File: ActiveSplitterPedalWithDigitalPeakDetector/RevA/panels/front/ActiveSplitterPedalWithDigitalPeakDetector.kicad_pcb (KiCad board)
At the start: 2 copper layers, 112.5 x 86.4 mm, 5 parts

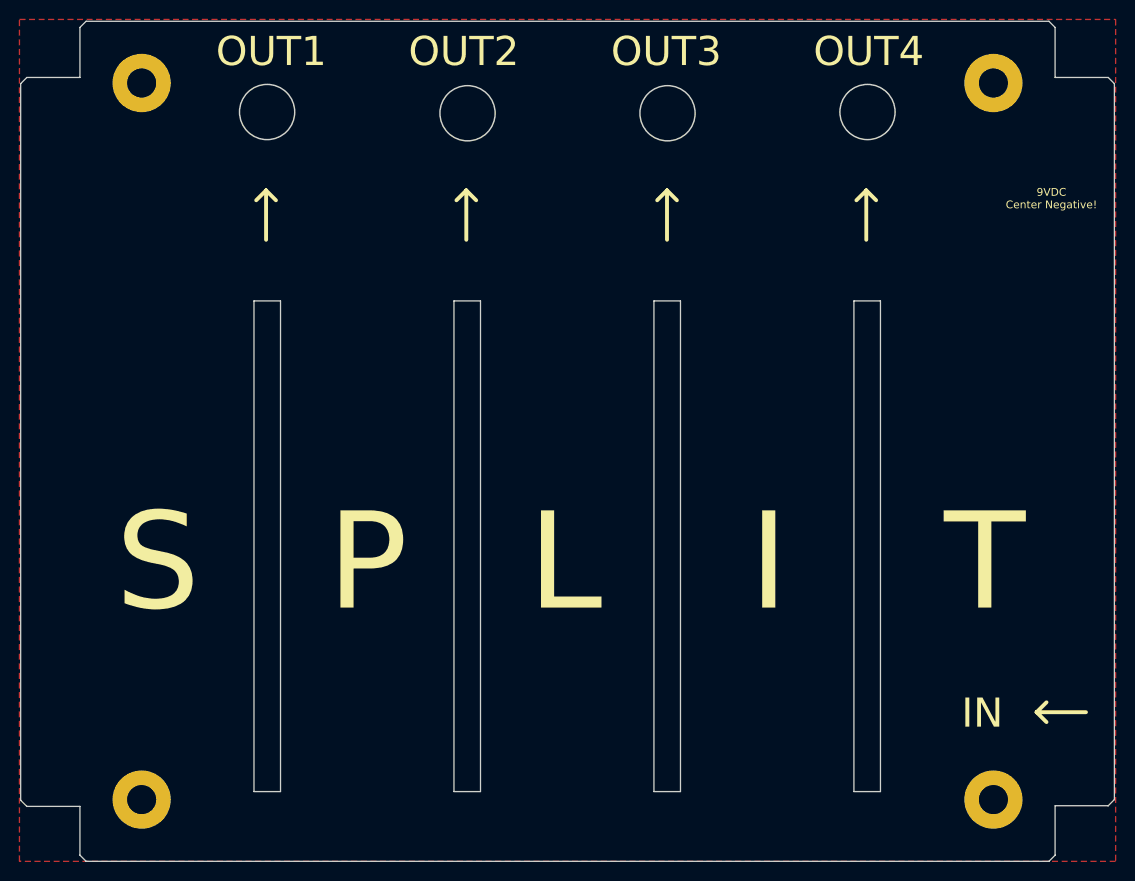
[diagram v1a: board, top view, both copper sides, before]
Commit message: updated front panel layout
moved silk screen
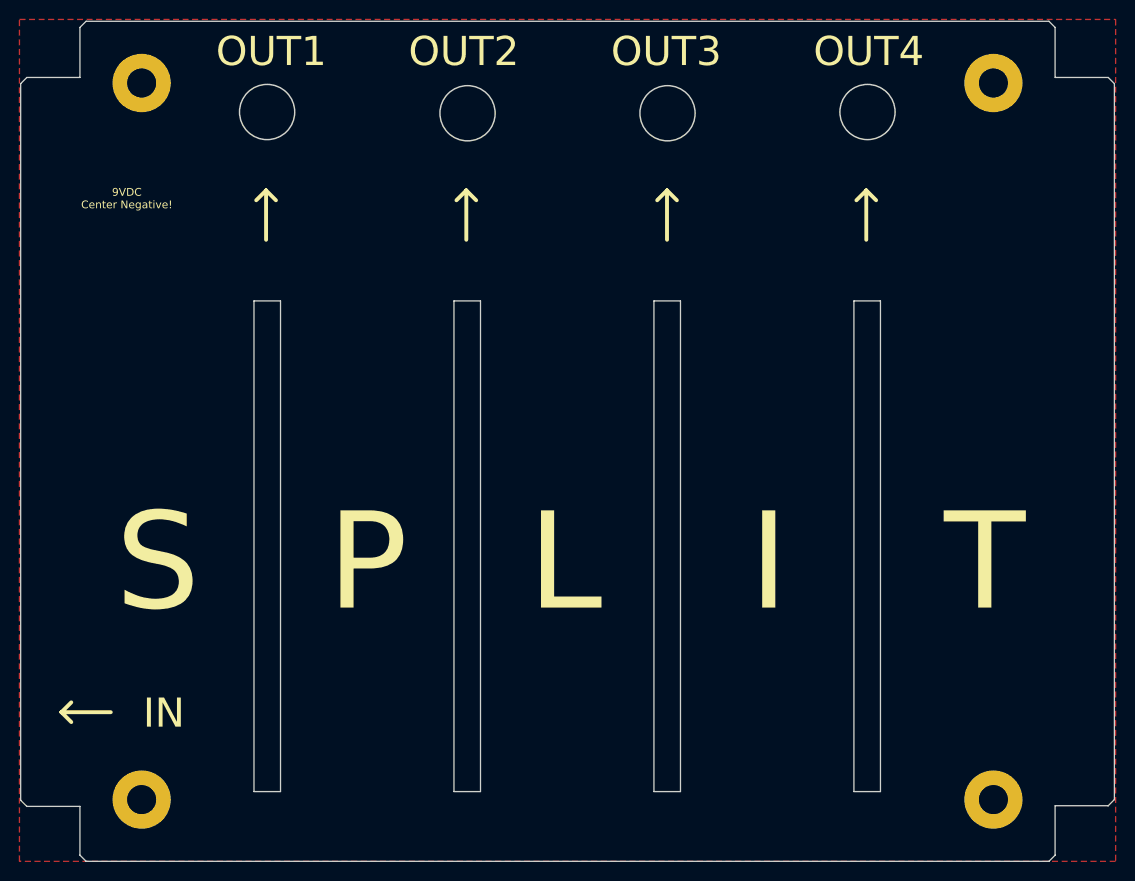
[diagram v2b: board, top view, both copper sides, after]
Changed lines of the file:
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@@
-(kicad_pcb (version 20171130) (host pcbnew "(5.1.6-0-10_14)")
+(kicad_pcb (version 20171130) (host pcbnew 5.1.6-c6e7f7d~87~ubuntu18.04.1)
   (general
     (thickness 1.6)
@@
       (effects (font (size 1 1) (thickness 0.15)))
     )
-    (fp_circle (center 0 0) (end 3.25 0) (layer F.CrtYd) (width 0.05))
-    (fp_circle (center 0 0) (end 3 0) (layer Cmts.User) (width 0.15))
+    (fp_circle (center 0 0) (end 3 0) (layer Cmts.User) (width 0.15))
+    (fp_circle (center 0 0) (end 3.25 0) (layer F.CrtYd) (width 0.05))
     (fp_text user %R (at 0.3 0) (layer F.Fab)
       (effects (font (size 1 1) (thickness 0.15)))
@@
       (effects (font (size 1 1) (thickness 0.15)))
     )
-    (fp_circle (center 0 0) (end 3.25 0) (layer F.CrtYd) (width 0.05))
-    (fp_circle (center 0 0) (end 3 0) (layer Cmts.User) (width 0.15))
+    (fp_circle (center 0 0) (end 3 0) (layer Cmts.User) (width 0.15))
+    (fp_circle (center 0 0) (end 3.25 0) (layer F.CrtYd) (width 0.05))
     (fp_text user %R (at 0.3 0) (layer F.Fab)
       (effects (font (size 1 1) (thickness 0.15)))
@@
       (effects (font (size 1 1) (thickness 0.15)))
     )
-    (fp_circle (center 0 0) (end 3.25 0) (layer F.CrtYd) (width 0.05))
-    (fp_circle (center 0 0) (end 3 0) (layer Cmts.User) (width 0.15))
+    (fp_circle (center 0 0) (end 3 0) (layer Cmts.User) (width 0.15))
+    (fp_circle (center 0 0) (end 3.25 0) (layer F.CrtYd) (width 0.05))
     (fp_text user %R (at 0.3 0) (layer F.Fab)
       (effects (font (size 1 1) (thickness 0.15)))
@@
       (effects (font (size 1 1) (thickness 0.15)))
     )
-    (fp_circle (center 0 0) (end 3.25 0) (layer F.CrtYd) (width 0.05))
-    (fp_circle (center 0 0) (end 3 0) (layer Cmts.User) (width 0.15))
+    (fp_circle (center 0 0) (end 3 0) (layer Cmts.User) (width 0.15))
+    (fp_circle (center 0 0) (end 3.25 0) (layer F.CrtYd) (width 0.05))
     (fp_text user %R (at 0.3 0) (layer F.Fab)
       (effects (font (size 1 1) (thickness 0.15)))
@@
       (effects (font (size 1 1) (thickness 0.15)))
     )
+    (fp_line (start 43.2435 -49.53) (end 42.6085 -50.165) (layer Dwgs.User) (width 0.12))
+    (fp_line (start 36.83 -56.261) (end 37.465 -55.626) (layer Dwgs.User) (width 0.12))
+    (fp_line (start -37.5285 -55.626) (end -36.8935 -56.261) (layer Dwgs.User) (width 0.12))
+    (fp_line (start -42.545 -50.165) (end -43.18 -49.53) (layer Dwgs.User) (width 0.12))
+    (fp_line (start -36.83 56.261) (end -37.465 55.626) (layer Dwgs.User) (width 0.12))
+    (fp_line (start -42.545 50.165) (end -43.18 49.53) (layer Dwgs.User) (width 0.12))
+    (fp_line (start 42.6085 50.165) (end 43.2435 49.53) (layer Dwgs.User) (width 0.12))
+    (fp_line (start 36.83 56.261) (end 37.465 55.626) (layer Dwgs.User) (width 0.12))
+    (fp_line (start -37.5285 -50.165) (end -42.545 -50.165) (layer Dwgs.User) (width 0.12))
+    (fp_line (start -37.5285 -55.626) (end -37.5285 -50.165) (layer Dwgs.User) (width 0.12))
+    (fp_line (start 37.465 -50.165) (end 37.465 -55.626) (layer Dwgs.User) (width 0.12))
+    (fp_line (start 42.6085 -50.165) (end 37.465 -50.165) (layer Dwgs.User) (width 0.12))
+    (fp_line (start 37.465 50.165) (end 42.6085 50.165) (layer Dwgs.User) (width 0.12))
+    (fp_line (start 37.465 55.626) (end 37.465 50.165) (layer Dwgs.User) (width 0.12))
+    (fp_line (start -37.465 50.165) (end -42.545 50.165) (layer Dwgs.User) (width 0.12))
+    (fp_line (start -37.465 55.626) (end -37.465 50.165) (layer Dwgs.User) (width 0.12))
+    (fp_line (start 43.2435 49.53) (end 43.2435 -49.53) (layer Dwgs.User) (width 0.12))
+    (fp_line (start -36.8935 -56.261) (end 36.83 -56.261) (layer Dwgs.User) (width 0.12))
+    (fp_line (start -36.83 56.261) (end 36.83 56.261) (layer Dwgs.User) (width 0.12))
+    (fp_line (start -43.18 49.53) (end -43.18 -49.53) (layer Dwgs.User) (width 0.12))
+    (fp_line (start -44.704 56.896) (end -44.704 -56.896) (layer Cmts.User) (width 0.12))
+    (fp_line (start 44.7675 56.896) (end -44.704 56.896) (layer Cmts.User) (width 0.12))
+    (fp_line (start 44.7675 -56.896) (end 44.7675 56.896) (layer Cmts.User) (width 0.12))
+    (fp_line (start -44.704 -56.896) (end 44.7675 -56.896) (layer Cmts.User) (width 0.12))
+    (fp_line (start -46.99 -59.7535) (end -46.99 59.7535) (layer Cmts.User) (width 0.12))
+    (fp_line (start 47.0535 59.7535) (end -46.99 59.7535) (layer Cmts.User) (width 0.12))
+    (fp_line (start -46.99 -59.7535) (end 47.0535 -59.7535) (layer Cmts.User) (width 0.12))
     (fp_line (start 47.0535 59.7535) (end 47.0535 -59.7535) (layer Cmts.User) (width 0.12))
-    (fp_line (start -46.99 -59.7535) (end 47.0535 -59.7535) (layer Cmts.User) (width 0.12))
-    (fp_line (start 47.0535 59.7535) (end -46.99 59.7535) (layer Cmts.User) (width 0.12))
-    (fp_line (start -46.99 -59.7535) (end -46.99 59.7535) (layer Cmts.User) (width 0.12))
-    (fp_line (start -44.704 -56.896) (end 44.7675 -56.896) (layer Cmts.User) (width 0.12))
-    (fp_line (start 44.7675 -56.896) (end 44.7675 56.896) (layer Cmts.User) (width 0.12))
-    (fp_line (start 44.7675 56.896) (end -44.704 56.896) (layer Cmts.User) (width 0.12))
-    (fp_line (start -44.704 56.896) (end -44.704 -56.896) (layer Cmts.User) (width 0.12))
-    (fp_line (start -43.18 49.53) (end -43.18 -49.53) (layer Dwgs.User) (width 0.12))
-    (fp_line (start -36.83 56.261) (end 36.83 56.261) (layer Dwgs.User) (width 0.12))
-    (fp_line (start -36.8935 -56.261) (end 36.83 -56.261) (layer Dwgs.User) (width 0.12))
-    (fp_line (start 43.2435 49.53) (end 43.2435 -49.53) (layer Dwgs.User) (width 0.12))
-    (fp_line (start -37.465 55.626) (end -37.465 50.165) (layer Dwgs.User) (width 0.12))
-    (fp_line (start -37.465 50.165) (end -42.545 50.165) (layer Dwgs.User) (width 0.12))
-    (fp_line (start 37.465 55.626) (end 37.465 50.165) (layer Dwgs.User) (width 0.12))
-    (fp_line (start 37.465 50.165) (end 42.6085 50.165) (layer Dwgs.User) (width 0.12))
-    (fp_line (start 42.6085 -50.165) (end 37.465 -50.165) (layer Dwgs.User) (width 0.12))
-    (fp_line (start 37.465 -50.165) (end 37.465 -55.626) (layer Dwgs.User) (width 0.12))
-    (fp_line (start -37.5285 -55.626) (end -37.5285 -50.165) (layer Dwgs.User) (width 0.12))
-    (fp_line (start -37.5285 -50.165) (end -42.545 -50.165) (layer Dwgs.User) (width 0.12))
-    (fp_line (start 36.83 56.261) (end 37.465 55.626) (layer Dwgs.User) (width 0.12))
-    (fp_line (start 42.6085 50.165) (end 43.2435 49.53) (layer Dwgs.User) (width 0.12))
-    (fp_line (start -42.545 50.165) (end -43.18 49.53) (layer Dwgs.User) (width 0.12))
-    (fp_line (start -36.83 56.261) (end -37.465 55.626) (layer Dwgs.User) (width 0.12))
-    (fp_line (start -42.545 -50.165) (end -43.18 -49.53) (layer Dwgs.User) (width 0.12))
-    (fp_line (start -37.5285 -55.626) (end -36.8935 -56.261) (layer Dwgs.User) (width 0.12))
-    (fp_line (start 36.83 -56.261) (end 37.465 -55.626) (layer Dwgs.User) (width 0.12))
-    (fp_line (start 43.2435 -49.53) (end 42.6085 -50.165) (layer Dwgs.User) (width 0.12))
   )
   (gr_line (start 105.1306 62.0395) (end 105.1306 67.1195) (layer F.SilkS) (width 0.4))
@@
   (gr_line (start 146.3802 62.0395) (end 145.3642 63.0555) (layer F.SilkS) (width 0.4))
   (gr_line (start 146.3802 62.0395) (end 147.3962 63.0555) (layer F.SilkS) (width 0.4))
-  (gr_text IN (at 178.816 115.824) (layer F.SilkS)
+  (gr_text IN (at 94.615 115.824) (layer F.SilkS)
     (effects (font (size 3 3) (thickness 0.4)))
   )
@@
   (gr_circle (center 125.857 54.102) (end 128.696806 54.102) (layer Edge.Cuts) (width 0.15))
   (gr_circle (center 105.237194 53.975) (end 108.077 53.975) (layer Edge.Cuts) (width 0.15))
-  (gr_text "9VDC\nCenter Negative!" (at 185.928 62.865) (layer F.SilkS)
+  (gr_text "9VDC\nCenter Negative!" (at 90.805 62.865) (layer F.SilkS)
     (effects (font (size 0.8 0.8) (thickness 0.15)))
   )
-  (gr_line (start 184.404 115.7224) (end 185.42 116.7384) (layer F.SilkS) (width 0.4))
-  (gr_line (start 184.404 115.7224) (end 189.484 115.7224) (layer F.SilkS) (width 0.4))
-  (gr_line (start 184.404 115.7224) (end 185.42 114.7064) (layer F.SilkS) (width 0.4))
+  (gr_line (start 84.074 115.7224) (end 85.09 116.7384) (layer F.SilkS) (width 0.4))
+  (gr_line (start 84.074 115.7224) (end 89.154 115.7224) (layer F.SilkS) (width 0.4))
+  (gr_line (start 84.074 115.7224) (end 85.09 114.7064) (layer F.SilkS) (width 0.4))
   (gr_text "MIrror, Negative for F.Cu layer\nMIrror, Negative for B.Cu layer" (at 134.239 26.035) (layer Cmts.User)
     (effects (font (size 1 1) (thickness 0.15)))
